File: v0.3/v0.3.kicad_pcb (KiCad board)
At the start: 4 copper layers, 47.4 x 50.5 mm, 94 parts, among them IC1 M95512-RMN6TP, IC2 TFBS4711-TT1, IC3 BQ25628ERYKR, IC4 RT6150B-33GQW, IC5 W25Q128JVSIM_TR, J1 USB4215-03-A, J2 SWD, J3 BAT, J4 DO0180FMST08, J5 UART, J6 SPEAKER_CONNECTOR, SW1 BUT_R, SW2 BUT_M, SW3 BUT_L, SW4 RUN, SW5 BOOTSEL, U1 RP2350A-QFN60, Y1 ABM8-272-T3, Y2 SIT1533AI-H4-DCC-32.768E

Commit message: v0.3: lots of routing done
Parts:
- R13, R14: moved to F.Cu
- SW1, SW2, SW3: footprint Button_Switch_SMD:SW_SPST_Omron_B3FS-101xP -> CustomFootprints:Button_membrane_5mm
- TH1: footprint Resistor_SMD:R_0402_1005Metric -> CustomFootprints:R_0402_1005Metric_Sunken
- moved R20 20.9 mm to (131.6, 111.8), turned to 180 degrees
- moved TH1 10.2 mm to (138.8, 105.4)
- moved C3 9.24 mm to (137.6, 79.4)
- moved R13 8.87 mm to (135.3, 111.2)
- moved R14 7.59 mm to (137.1, 110.2), turned to 90 degrees
- moved R5 7.49 mm to (142.9, 79.0)
- moved R18 7.13 mm to (136.1, 111.9), turned to 0 degrees
- moved C2 3.85 mm to (142.9, 78.0), turned to 0 degrees
- moved R6 3.76 mm to (138.0, 78.1), turned to 0 degrees
- moved C27 3.52 mm to (146.5, 98.0)
- moved C4 3.37 mm to (124.5, 103.0), turned to 0 degrees
- moved C1 2.60 mm to (123.2, 97.5)
- moved C5 2.55 mm to (123.9, 98.5), turned to 180 degrees
- moved R3 2.55 mm to (128.1, 97.5)
- moved R24 2.47 mm to (132.1, 99.5), turned to 90 degrees
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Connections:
- AC1 pad 3: /accel/ACCEL_3V3 -> +3.3V
- AC1 pad 7: /accel/ACCEL_3V3 -> +3.3V
- C1 pad 1: /eeprom/EEPROM_3V3 -> +3.3V
- C19 pad 2: /screen/SCREEN_VSYS -> VSYS
- C20 pad 1: /screen/SCREEN_VSYS -> VSYS
- C21 pad 1: /screen/SCREEN_3V3 -> +3.3V
- C27 pad 1: /mcu/MCU_3V3 -> +3.3V
- C28 pad 1: /mcu/MCU_3V3 -> +3.3V
- C29 pad 1: /mcu/MCU_3V3 -> +3.3V
- C30 pad 1: /mcu/MCU_3V3 -> +3.3V
- C31 pad 1: /mcu/MCU_3V3 -> +3.3V
- C32 pad 1: /mcu/MCU_3V3 -> +3.3V
- C33 pad 1: /mcu/MCU_3V3 -> +3.3V
- C35 pad 1: /mcu/MCU_3V3 -> +3.3V
- C39 pad 1: /flash/FLASH_3V3 -> +3.3V
- C4 pad 1: /accel/ACCEL_3V3 -> +3.3V
- C40 pad 1: /flash/FLASH_3V3 -> +3.3V
- C5 pad 1: /accel/ACCEL_3V3 -> +3.3V
- IC1 pad 3: /eeprom/EEPROM_3V3 -> +3.3V
- IC1 pad 7: /eeprom/EEPROM_3V3 -> +3.3V
- IC1 pad 8: /eeprom/EEPROM_3V3 -> +3.3V
- IC3 pad 11: /power/PWR_AUX.~{BAT_INT} -> /mcu/PWR_AUX.~{BAT_INT}
- IC3 pad 14: /power/PWR_AUX.~{BAT_CE} -> /mcu/PWR_AUX.~{BAT_CE}
- IC3 pad 22: /power/PWR_AUX.~{BAT_CE} -> /mcu/PWR_AUX.~{BAT_CE}
- IC3 pad 3: /power/PWR_AUX.~{PG} -> /mcu/PWR_AUX.~{PG}
- IC5 pad 8: /flash/FLASH_3V3 -> +3.3V
- J3 pad 2: GND -> /screen/SCREEN_3V3
- J4 pad 17: /screen/SCREEN_3V3 -> +3.3V
- J4 pad 18: /screen/SCREEN_VSYS -> VSYS
- J4 pad 20: /screen/SCREEN_VSYS -> VSYS
- J4 pad 24: /screen/SCREEN_3V3 -> +3.3V
- J4 pad 26: /screen/SCREEN_3V3 -> +3.3V
- R20 pad 2: /power/PWR_AUX.~{PG} -> /mcu/PWR_AUX.~{PG}
- R3 pad 1: /eeprom/EEPROM_3V3 -> +3.3V
- R33 pad 1: /mcu/MCU_3V3 -> +3.3V
- R5 pad 1: /irda/IRDA_3V3 -> +3.3V
- R6 pad 1: /irda/IRDA_3V3 -> +3.3V
- U1 pad 1: /mcu/MCU_3V3 -> +3.3V
- U1 pad 10: /mcu/SCREEN_AUX.~{CSB} -> /mcu/SCREEN_AUX.~{RST}
- U1 pad 11: /mcu/MCU_3V3 -> +3.3V
- U1 pad 20: /mcu/MCU_3V3 -> +3.3V
- U1 pad 30: /mcu/MCU_3V3 -> +3.3V
- U1 pad 38: /mcu/MCU_3V3 -> +3.3V
- U1 pad 40: /mcu/PWR_AUX.~{BAT_INT} -> /mcu/PWR_AUX.~{BAT_CE}
- U1 pad 41: /mcu/PWR_AUX.~{BAT_CE} -> /mcu/PWR_AUX.~{BAT_INT}
- U1 pad 44: /mcu/MCU_3V3 -> +3.3V
- U1 pad 45: /mcu/MCU_3V3 -> +3.3V
- U1 pad 49: /mcu/MCU_3V3 -> +3.3V
- U1 pad 53: /mcu/MCU_3V3 -> +3.3V
- U1 pad 54: /mcu/MCU_3V3 -> +3.3V
- U1 pad 9: /mcu/SCREEN_AUX.~{RST} -> /mcu/SCREEN_AUX.~{CSB}
- Y2 pad 4: /mcu/MCU_3V3 -> +3.3V
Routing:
- net +3.3V: track 0.00 -> 99.1 mm, vias 0 -> 24
- net /accel/SPI.MOSI: track 0.00 -> 34.0 mm
- net /accel/SPI.MISO: track 0.00 -> 34.0 mm, vias 0 -> 2
- net /mcu/PWR_AUX.~{PG}: track 0.00 -> 33.0 mm, vias 0 -> 2
- net /accel/SPI.SCK: track 0.00 -> 31.3 mm
- net /mcu/SOUND_PWM: track 0.00 -> 27.6 mm, vias 0 -> 1
- net /mcu/MCU_1V1: track 0.00 -> 26.8 mm, vias 0 -> 8
- net /power/~{STAT}: track 0.72 -> 26.3 mm, vias 1 -> 2
- net GND: track 0.00 -> 23.7 mm, vias 0 -> 80
- net /buttons/BUT.R: track 0.00 -> 23.1 mm, vias 0 -> 2
- net /connectors/USB.D+: track 0.00 -> 22.8 mm, vias 0 -> 1
- net /connectors/DBG_UART.RX: track 0.00 -> 20.6 mm, vias 0 -> 2
- net /connectors/DBG_UART.TX: track 0.00 -> 20.5 mm, vias 0 -> 2
- net /flash/QSPI0.SS: track 0.00 -> 19.9 mm
- net /connectors/USB.D-: track 0.00 -> 19.9 mm, vias 0 -> 1
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- added copper zone on B.Cu, net +3.3V
- added copper zone on F.Cu, net +3.3V
- added copper zone on In2.Cu, net +3.3V
- added copper zone on F.Cu, net /connectors/BAT+
- added copper zone on F.Cu, net /mcu/MCU_1V1
- added copper zone on F.Cu, net /mcu/VREG_LX
- added copper zone on F.Cu, net /power/PMID
- added copper zone on F.Cu, net /power/REGN
- added copper zone on F.Cu, net /power/SW
- added copper zone on B.Cu, net GND
- added copper zone on F.Cu, net GND
- added copper zone on In1.Cu, net GND
- added copper zone on In2.Cu, net VBUS
- added copper zone on F.Cu, net VSYS
- removed copper zone on In2.Cu, net (none)
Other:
- outline, holes or cut-outs redrawn

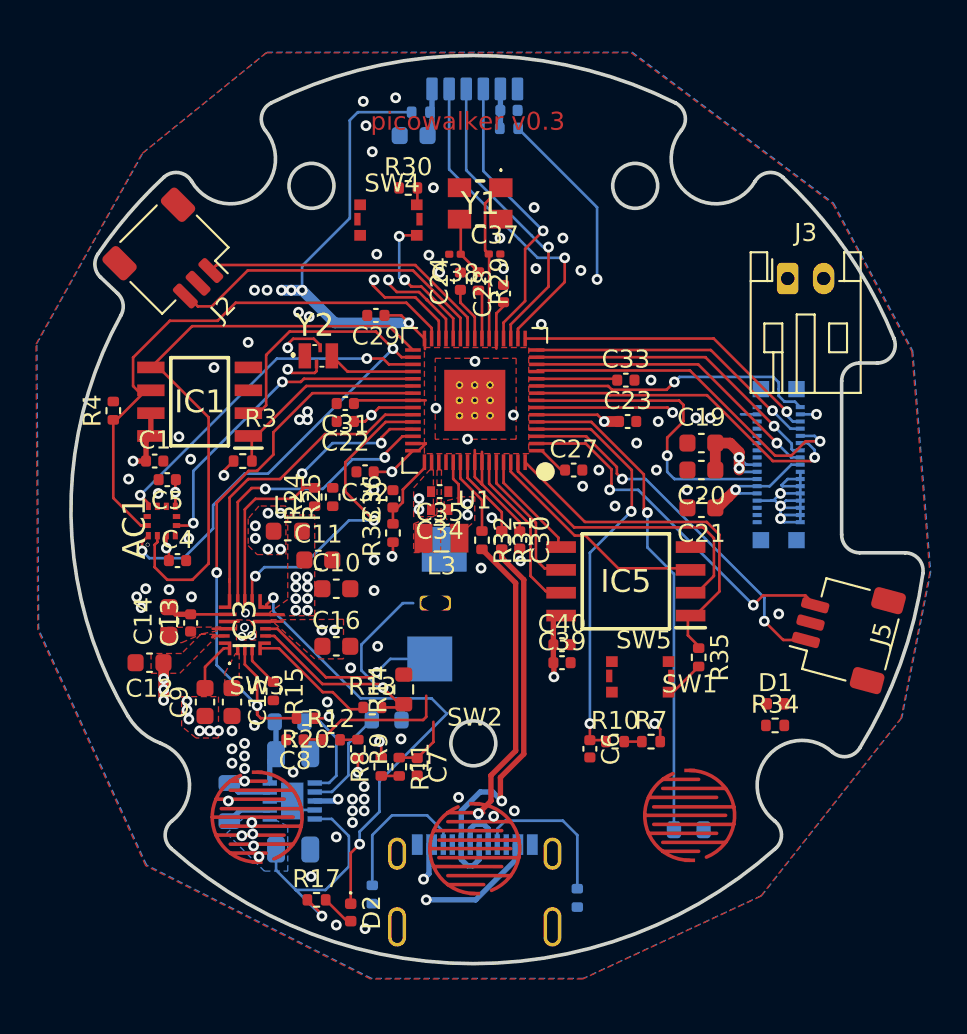
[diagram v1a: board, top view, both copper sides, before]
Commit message: v0.3: move pmic to right side of board
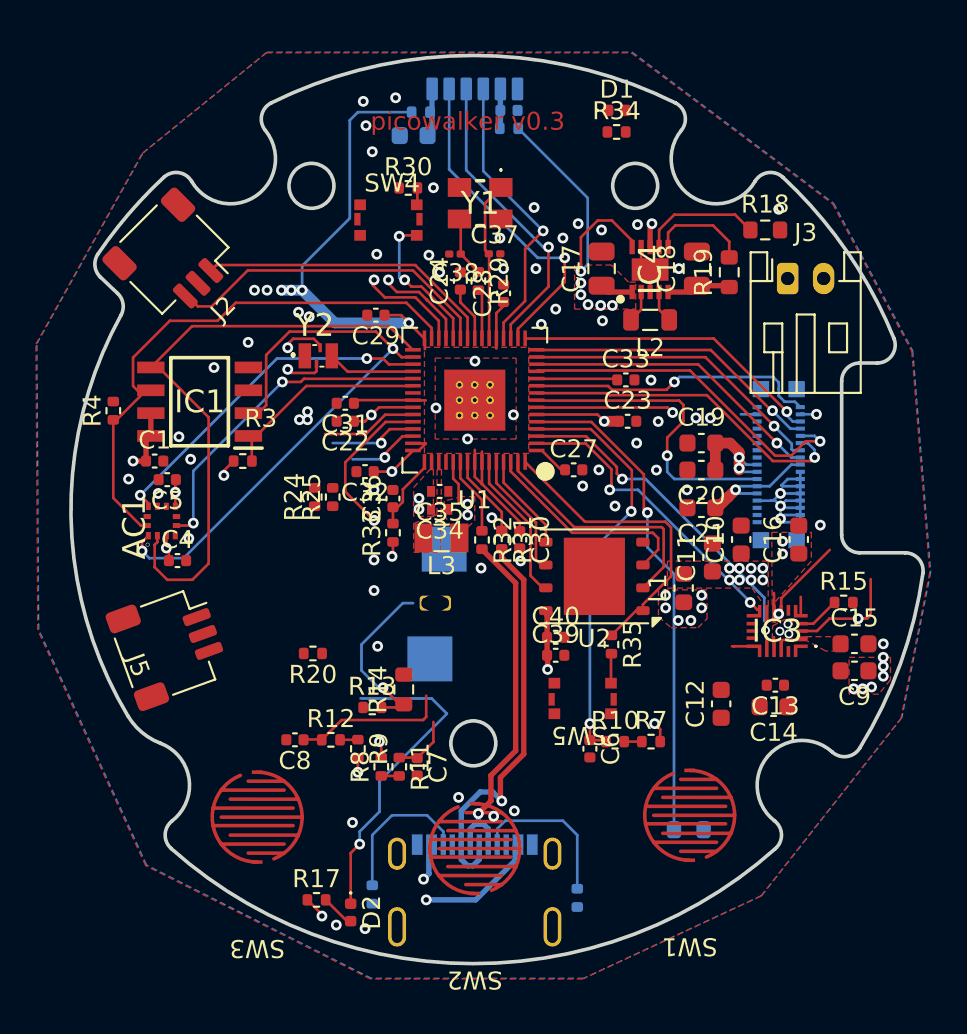
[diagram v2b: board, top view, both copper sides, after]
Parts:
- removed IC5: W25Q128JVSIM_TR, SamacSys_Parts:SOIC127P790X216-8N
- added U2: W25Q128JVP, Package_SON:WSON-8-1EP_6x5mm_P1.27mm_EP3.4x4.3mm, F.Cu at (147.7, 103.9)
- C17, C18, IC4, L2, R18, R19: moved to F.Cu
- moved J5 37.6 mm to (124.0, 107.8), turned to -70 degrees
- moved C17 36.6 mm to (148.1, 86.8), turned to 90 degrees
- moved C9 36.2 mm to (162.1, 109.2), turned to 180 degrees
- moved IC4 35.6 mm to (150.8, 86.8), turned to 90 degrees
- moved L2 35.6 mm to (150.8, 89.7), turned to 180 degrees
- moved C18 35.1 mm to (153.3, 86.8), turned to 90 degrees
- moved R19 35.0 mm to (155.2, 87.0), turned to 90 degrees
- moved C15 34.8 mm to (162.1, 107.7), turned to 0 degrees
- moved R18 34.4 mm to (157.2, 84.7)
- moved D1 34.2 mm to (148.9, 78.0)
- moved R34 34.2 mm to (148.9, 79.2)
- moved C14 34.0 mm to (157.6, 111.2), turned to 180 degrees
- moved C13 32.7 mm to (157.7, 110.0), turned to 180 degrees
- moved R15 32.1 mm to (161.5, 105.4), turned to 0 degrees
- moved C12 31.9 mm to (154.7, 111.0), turned to 90 degrees
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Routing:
- net /mcu/PWR_AUX.~{PG}: track 33.0 -> 6.58 mm, vias 2 -> 1
- net /mcu/I2C.SCL: track 16.9 -> 4.01 mm, vias 2 -> 1
- net /mcu/I2C.SDA: track 17.7 -> 4.96 mm, vias 2 -> 1
- net /mcu/PWR_AUX.~{BAT_CE}: track 18.0 -> 6.56 mm
- net /mcu/PWR_AUX.~{BAT_INT}: track 17.8 -> 8.59 mm, vias 2 -> 1
- net /power/TS: track 17.6 -> 9.85 mm
- net /power/~{STAT}: track 26.3 -> 18.6 mm
- net /power/~{QON}: track 10.8 -> 4.48 mm, vias 1 -> 0
- net /power/TS_BIAS: track 7.13 -> 1.05 mm
- net +3.3V: track 99.1 -> 93.1 mm
- net /connectors/DBG_UART.TX: track 20.5 -> 16.6 mm, vias 2 -> 1
- net GND: track 23.7 -> 20.3 mm, vias 80 -> 68
- net /flash/QSPI0.SD1: track 16.8 -> 13.7 mm
- net /power/BTST: track 2.97 -> 0.00 mm
- net VBUS: track 11.7 -> 8.86 mm, vias 5 -> 2
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- removed copper zone on B.Cu, net +3.3V
- removed copper zone on In2.Cu, net /connectors/BAT+
- removed copper zone on F.Cu, net /power/PMID
- removed copper zone on F.Cu, net VBUS
- removed copper zone on In2.Cu, net VBUS

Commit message: v0.3: DRC checks mostly pass, onto final tweaks
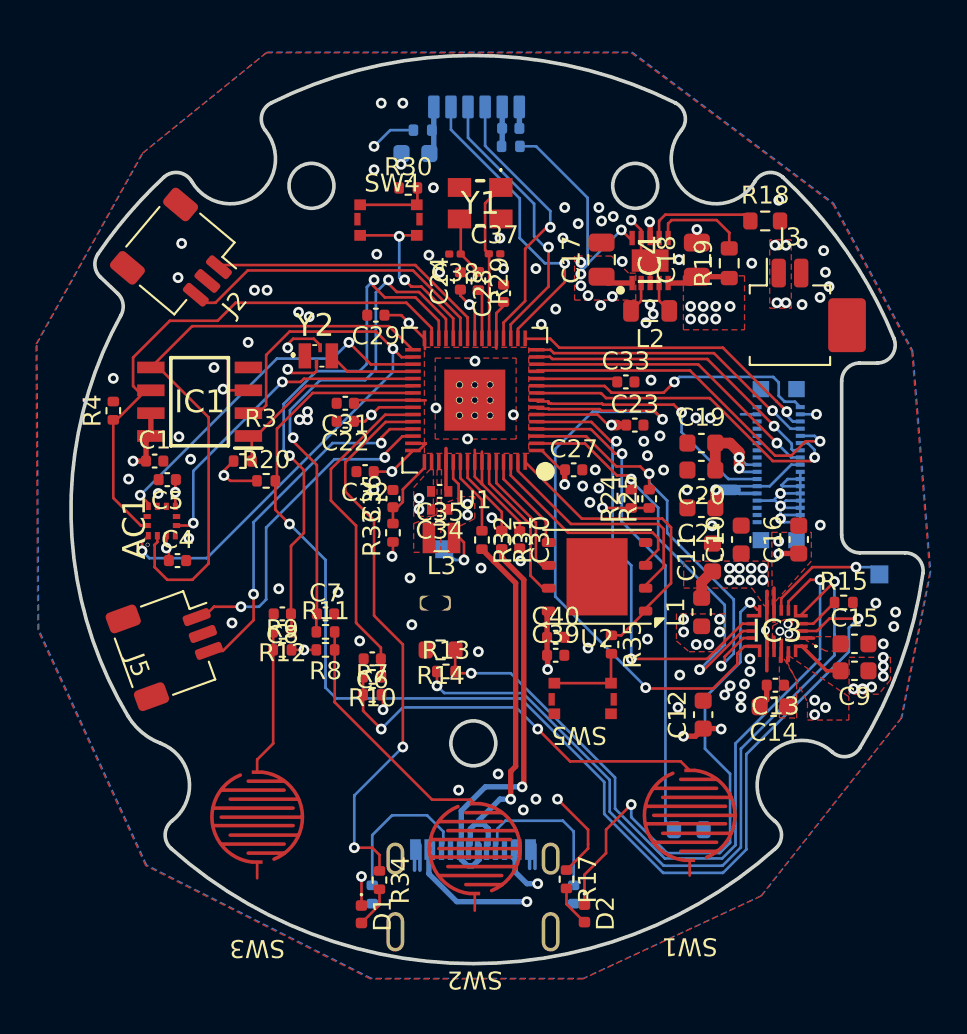
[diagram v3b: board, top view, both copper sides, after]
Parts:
- J3: footprint Connector_JST:JST_PH_S2B-PH-K_1x02_P2.00mm_Horizontal -> Connector_Molex:Molex_PicoBlade_53261-0271_1x02-1MP_P1.25mm_Horizontal
- TP1, TP2: footprint TestPoint:TestPoint_Pad_2.5x2.5mm -> TestPoint:TestPoint_Pad_1.0x1.0mm
- moved D1 46.9 mm to (134.7, 122.7), turned to -90 degrees
- moved R34 43.6 mm to (135.7, 120.8), turned to -90 degrees
- moved TP1 25.4 mm to (163.5, 103.8)
- moved R24 17.6 mm to (149.7, 99.6)
- moved R25 17.6 mm to (150.7, 99.6)
- moved R7 15.7 mm to (135.3, 110.5)
- moved R10 14.0 mm to (135.3, 109.5), turned to 180 degrees
- moved R17 13.9 mm to (146.1, 120.8), turned to -90 degrees
- moved C6 13.1 mm to (135.3, 108.5), turned to 180 degrees
- moved D2 13.0 mm to (147.1, 122.7)
- moved R20 9.95 mm to (129.4, 98.6), turned to 0 degrees
- moved C7 9.91 mm to (132.7, 106.0), turned to 0 degrees
- moved R11 8.55 mm to (132.7, 107.0), turned to 0 degrees
- moved R8 7.20 mm to (132.7, 108.0), turned to 180 degrees
- moved C8 7.03 mm to (130.3, 106.0)
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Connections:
- J3 pad 2: /screen/SCREEN_3V3 -> GND
- U1 pad 2: /connectors/DBG_UART.TX -> /mcu/I2C.SDA
- U1 pad 3: /connectors/DBG_UART.RX -> /mcu/I2C.SCL
- U1 pad 4: /buttons/BUT.R -> /mcu/SOUND_PWM
- U1 pad 40: /mcu/PWR_AUX.~{BAT_CE} -> /buttons/BUT.R
- U1 pad 41: /mcu/PWR_AUX.~{BAT_INT} -> /mcu/USER_LED
- U1 pad 42: /mcu/I2C.SDA -> /connectors/DBG_UART.TX
- U1 pad 43: /mcu/I2C.SCL -> /connectors/DBG_UART.RX
- U1 pad 5: /mcu/SOUND_PWM -> /mcu/PWR_AUX.~{BAT_INT}
- U1 pad 7: /mcu/USER_LED -> /mcu/PWR_AUX.~{BAT_CE}
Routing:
- net /mcu/PWR_AUX.~{PG}: track 6.58 -> 71.7 mm, vias 1 -> 2
- net /power/TS_BIAS: track 1.05 -> 42.9 mm, vias 0 -> 2
- net /power/TS: track 9.85 -> 41.9 mm, vias 1 -> 2
- net /mcu/PWR_AUX.~{BAT_CE}: track 6.56 -> 37.0 mm, vias 0 -> 2
- net /mcu/USER_LED: track 7.68 -> 31.1 mm, vias 1 -> 2
- net /buttons/BUT_R_1: track 0.98 -> 22.4 mm, vias 0 -> 2
- net /buttons/BUT.M: track 8.79 -> 29.3 mm, vias 1 -> 2
- net /mcu/I2C.SCL: track 4.01 -> 23.6 mm, vias 1 -> 2
- net /mcu/I2C.SDA: track 4.96 -> 23.8 mm, vias 1 -> 2
- net GND: track 20.3 -> 37.0 mm, vias 68 -> 104
- net /mcu/PWR_AUX.~{BAT_INT}: track 8.59 -> 25.1 mm, vias 1 -> 2
- net /buttons/BUT.L: track 14.3 -> 29.6 mm, vias 1 -> 2
- net /buttons/BUT_M_1: track 1.00 -> 14.0 mm
- net /power/~{STAT}: track 18.6 -> 29.6 mm
- net +3.3V: track 93.1 -> 83.6 mm
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- added copper zone on In2.Cu, net /connectors/BAT+
- added copper zone on F.Cu, net /power/PMID
- added copper zone on F.Cu, net VBUS
- added copper zone on In2.Cu, net VBUS
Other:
- board text added: "picowalker v0.3 Design and PCB: mamba2410 Shell and mechanical: Kamp Logo: Zenith"

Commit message: v0.3: moved everything down a bit to better fit voltage reg
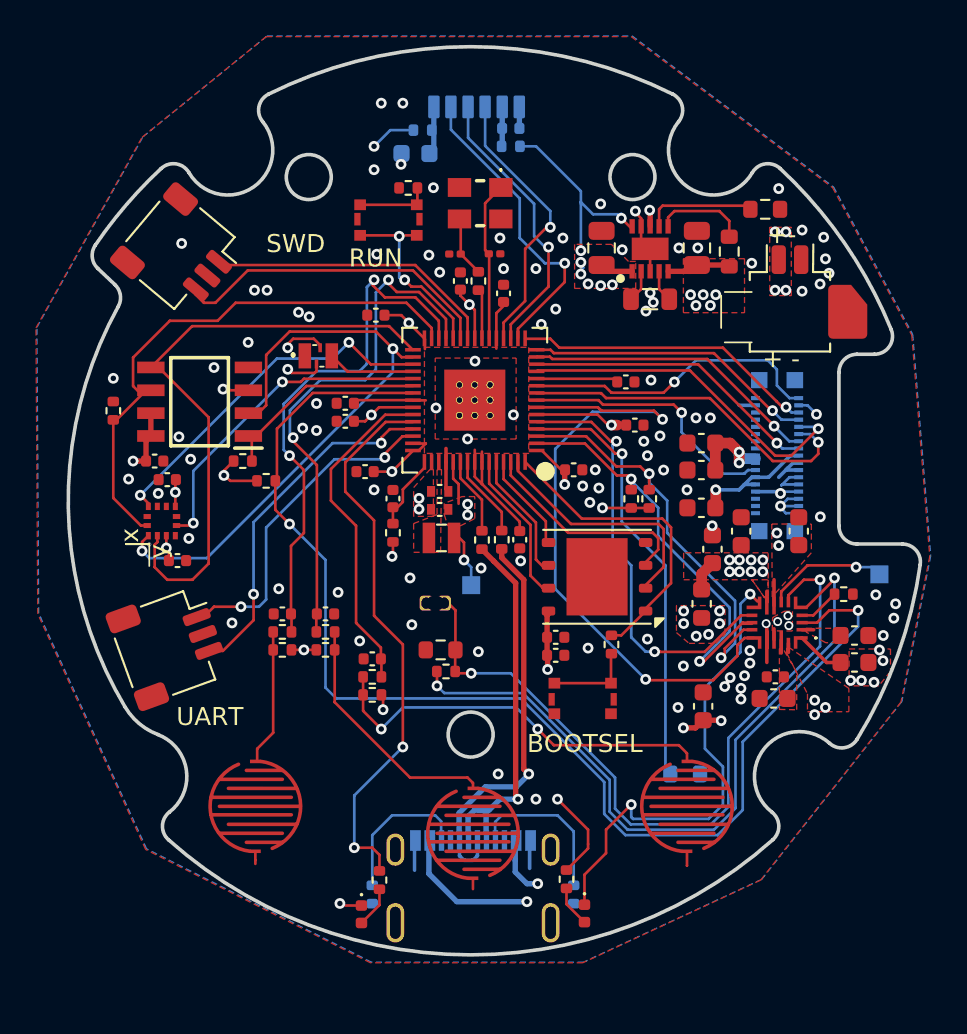
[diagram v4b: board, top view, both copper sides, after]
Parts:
- AC1: footprint SamacSys_Parts:BOSCH_LGA-12 -> CustomFootprints:BOSCH_LGA-12_BMA400
- moved J6 3.11 mm to (152.7, 114.9)
- moved TP2 2.50 mm to (140.8, 104.4)
- moved SW2 0.86 mm to (140.9, 118.2)
- moved J3 0.74 mm to (158.5, 88.7)
- moved L2 0.65 mm to (150.8, 88.5)
- moved R18 0.65 mm to (157.2, 83.5)
- moved R19 0.65 mm to (155.2, 85.8)
- moved C17 0.65 mm to (148.1, 85.7)
- moved C18 0.65 mm to (153.3, 85.7)
- moved IC4 0.65 mm to (150.8, 85.7)
- moved SW3 0.61 mm to (128.8, 116.7)
- moved SW1 0.52 mm to (152.8, 116.7)
- moved J4 0.51 mm to (157.8, 97.2)
- moved J1 0.50 mm to (140.9, 118.6)
- moved C13 0.46 mm to (157.7, 109.5)
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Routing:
- net GND: track 37.0 -> 28.6 mm, vias 104 -> 95
- net /mcu/SOUND_PWM: track 27.4 -> 24.2 mm
- net /power/TS_BIAS: track 42.9 -> 39.9 mm
- net /power/~{STAT}: track 29.6 -> 26.7 mm
- net /mcu/PWR_AUX.~{PG}: track 71.7 -> 69.0 mm
- net +3.3V: track 83.6 -> 81.3 mm
- net VSYS: track 19.6 -> 17.8 mm, vias 18 -> 16
- net /connectors/BAT+: track 2.56 -> 1.44 mm
- net /mcu/SCREEN_AUX.~{CSB}: track 18.5 -> 19.3 mm
- net /mcu/PWR_AUX.~{BAT_INT}: track 25.1 -> 24.2 mm
- net /buttons/BUT_L_1: track 8.17 -> 7.47 mm
- net /power/TS: track 41.9 -> 41.3 mm
- net /mcu/SCREEN_AUX.~{RST}: track 16.3 -> 16.9 mm
- net /connectors/USB.D+: track 22.5 -> 22.0 mm
- net /power/SW: vias 15 -> 14
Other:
- board text added: "+ -"
- board text added: "+-"
- board text added: "BOOTSEL"
- board text added: "MCU_1V1"
- board text added: "RUN"
- board text added: "SWD"
- board text added: "UART"
- board text added: "~{QON}"
